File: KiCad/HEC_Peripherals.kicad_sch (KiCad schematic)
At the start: 11 parts, among them J2 Conn_02x12_Odd_Even, J4 Mini-DIN-6, J5 Mini-DIN-6, J6 DE9_Plug, J7 AudioJack3, U43 74LS06, U44 74LS541, Y1 Crystal

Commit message: Add NES port
Added NES port from NES port breadboard project
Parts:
- added C31, C32: C, Capacitor_THT:C_Disc_D3.4mm_W2.1mm_P2.50mm, symbol Device:C
- added J8: NES_Port_Male, Library:NES_Port_Male_Horizontal, symbol nes-port-breadboard:NES_Port_Male
- U42: footprint (none) -> Package_DIP:DIP-40_W25.4mm_Socket
- U43: footprint (none) -> Package_DIP:DIP-14_W7.62mm_Socket
- U44: footprint (none) -> Package_DIP:DIP-20_W7.62mm_Socket
- Y1: footprint (none) -> Crystal:Crystal_HC18-U_Vertical
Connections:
- net GND: now also C31.1, C32.1, J8.1 (GND)
- net VCC: now also J8.7 (VDD)
- net at U42.2 (OSCI), Y1.1: now also C31.2
- net at U42.3 (OSCO), Y1.2: now also C32.2
- net at U42.21 (RC): now also J8.2 (CLK)
- net at U42.22 (A20): now also J8.3 (LATCH)
- net at U42.29 (P12): now also J8.4 (DATA)
- net at U42.30 (P13): now also J8.5 (D4)
- net at U42.31 (P14): now also J8.6 (D3)
- no-connect marks 11 -> 6
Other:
- moved on the sheet: J4, J5, RN5, U43A, U43B, U43C, U43D

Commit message: Removed DMA from bus
Bus-mastering DMA has been removed from the expansion bus design due to complexity and bandwidth issue with external bus expansion circuit. The pins are replaced with audio output from on-bard sound system. Minor changes to pin names.
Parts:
- removed J8: NES_Port_Male, Library:NES_Port_Male_Horizontal, symbol nes-port-breadboard:NES_Port_Male
- added J8: NES_Port_Male, symbol New_Library:NES_Port_Male
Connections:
- net GND: now also J8.1 (GND)
- net VCC: now also J8.7 (VDD)
- net AUDIO_R: now reaches J2.23 (Pin_23), J7.T
- net AUDIO_L: now reaches J2.24 (Pin_24), J7.R
- net at U42.21 (RC): now also J8.2 (CLK)
- net at U42.22 (A20): now also J8.3 (LATCH)
- net at U42.29 (P12): now also J8.4 (DATA)
- net at U42.30 (P13): now also J8.5 (D4)
- net at U42.31 (P14): now also J8.6 (D3)
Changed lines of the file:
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@@
   (junction (at 66.675 160.02) (diameter 0) (color 0 0 0 0)
   )
+  (junction (at 74.93 95.885) (diameter 0) (color 0 0 0 0)
+  )
   (junction (at 76.835 170.18) (diameter 0) (color 0 0 0 0)
   )
@@
   )
   (junction (at 71.755 165.1) (diameter 0) (color 0 0 0 0)
+  )
+  (junction (at 90.805 93.345) (diameter 0) (color 0 0 0 0)
   )
   (junction (at 241.3 84.455) (diameter 0) (color 0 0 0 0)
@@
     (stroke (width 0) (type default))
   )
-  (wire (pts (xy 98.425 95.885) (xy 74.93 95.885))
+  (wire (pts (xy 71.755 95.885) (xy 74.93 95.885))
     (stroke (width 0) (type default))
   )
@@
     (stroke (width 0) (type default))
   )
+  (wire (pts (xy 71.755 93.345) (xy 90.805 93.345))
+    (stroke (width 0) (type default))
+  )
   (wire (pts (xy 52.07 167.64) (xy 74.295 167.64))
     (stroke (width 0) (type default))
@@
   )
   (wire (pts (xy 133.35 96.52) (xy 133.35 104.14))
+    (stroke (width 0) (type default))
+  )
+  (wire (pts (xy 74.93 95.885) (xy 98.425 95.885))
     (stroke (width 0) (type default))
   )
@@
     (effects (font (size 1.27 1.27)) (justify right))
   )
+  (hierarchical_label "AUDIO_L" (shape output) (at 71.755 93.345 180) (fields_autoplaced)
+    (effects (font (size 1.27 1.27)) (justify right))
+  )
   (hierarchical_label "A[0..4]" (shape input) (at 41.275 56.515 180) (fields_autoplaced)
     (effects (font (size 1.27 1.27)) (justify right))
@@
   )
   (hierarchical_label "~{MS_IRQ}" (shape output) (at 129.54 90.17 180) (fields_autoplaced)
+    (effects (font (size 1.27 1.27)) (justify right))
+  )
+  (hierarchical_label "AUDIO_R" (shape output) (at 71.755 95.885 180) (fields_autoplaced)
     (effects (font (size 1.27 1.27)) (justify right))
   )
@@
     )
   )
+  (symbol (lib_id "New_Library:NES_Port_Male") (at 210.82 33.655 0) (unit 1)
+    (in_bom yes) (on_board yes) (dnp no) (fields_autoplaced)
+    (property "Reference" "J8" (at 210.82 24.13 0)
+      (effects (font (size 1.27 1.27)))
+    )
+    (property "Value" "NES_Port_Male" (at 210.82 26.67 0)
+      (effects (font (size 1.27 1.27)))
+    )
+    (property "Footprint" "" (at 238.76 31.115 0)
+      (effects (font (size 1.27 1.27)) hide)
+    )
+    (property "Datasheet" "" (at 238.76 31.115 0)
+      (effects (font (size 1.27 1.27)) hide)
+    )
+    (pin "1")
+    (pin "2")
+    (pin "3")
+    (pin "4")
+    (pin "5")
+    (pin "6")
+    (pin "7")
+    (instances
+      (project "HEC1"
+        (path "/87935374-b60a-4f41-99da-94b76103dd77/b96e4e19-77bb-438e-a98c-e547a5bf0bc4"
+          (reference "J8") (unit 1)
+        )
+      )
+    )
+  )
   (symbol (lib_id "power:GND") (at 189.23 36.195 0) (unit 1)
     (in_bom yes) (on_board yes) (dnp no) (fields_autoplaced)
@@
         )
       )
-    )
-  )
-  (symbol (lib_id "nes-port-breadboard:NES_Port_Male") (at 210.82 33.655 0) (unit 1)
-    (in_bom yes) (on_board yes) (dnp no) (fields_autoplaced)
-    (property "Reference" "J8" (at 210.82 23.495 0)
-      (effects (font (size 1.27 1.27)))
-    )
-    (property "Value" "NES_Port_Male" (at 210.82 26.035 0)
-      (effects (font (size 1.27 1.27)))
-    )
-    (property "Footprint" "Library:NES_Port_Male_Horizontal" (at 238.76 31.115 0)
-      (effects (font (size 1.27 1.27)) hide)
-    )
-    (property "Datasheet" "" (at 238.76 31.115 0)
-      (effects (font (size 1.27 1.27)) hide)
-    )
-    (pin "1")
-    (pin "2")
-    (pin "3")
-    (pin "4")
-    (pin "5")
-    (pin "6")
-    (pin "7")
-    (instances
-      (project "HEC1"
-        (path "/87935374-b60a-4f41-99da-94b76103dd77/b96e4e19-77bb-438e-a98c-e547a5bf0bc4"
-          (reference "J8") (unit 1)
-        )
-      )

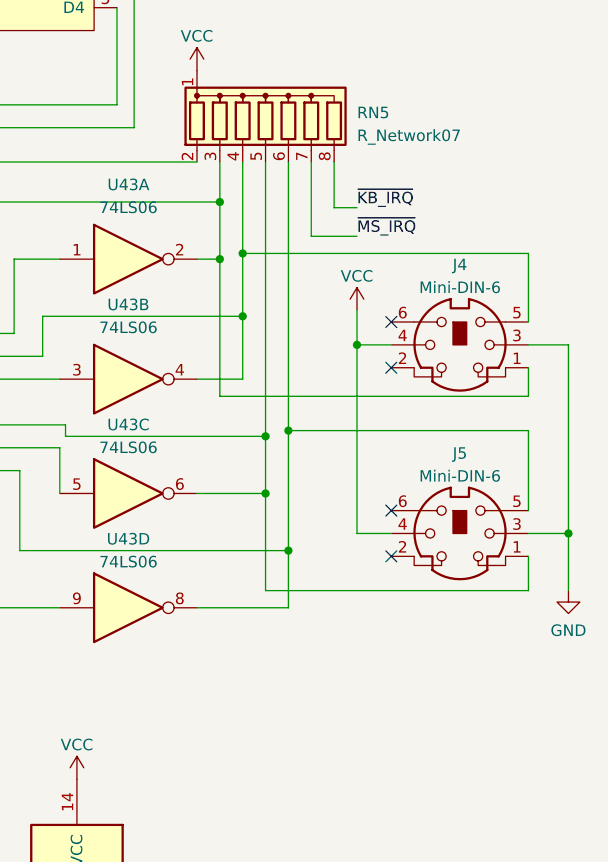
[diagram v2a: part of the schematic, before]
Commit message: Add Mini-DIN-6 footprint
It turns out that KiCad had only symbol but not footprint for Mini-DIN-6. Therefore I used a custom one made by 4x1md
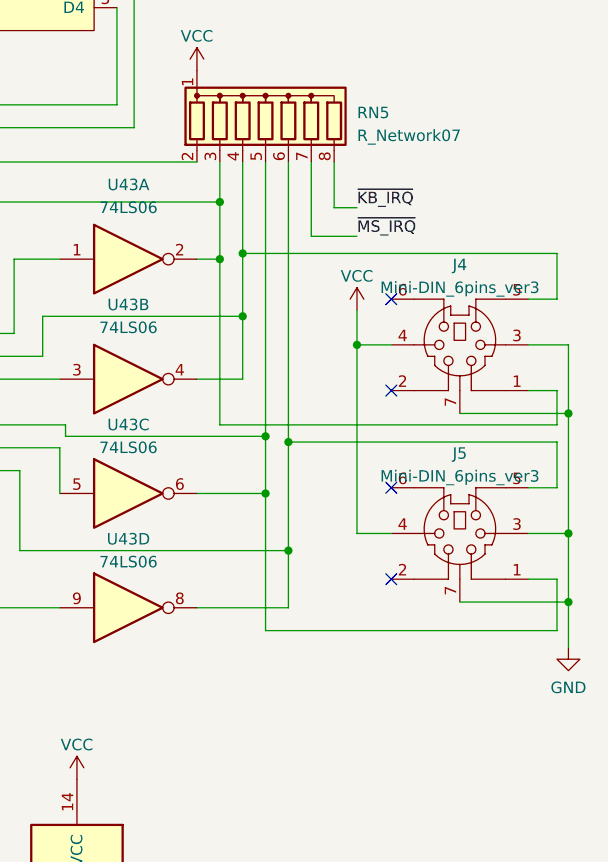
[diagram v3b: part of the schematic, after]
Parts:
- removed J4, J5: Mini-DIN-6, symbol Connector:Mini-DIN-6
- added J4, J5: Mini-DIN_6pins_ver3, Library:Connector_Mini-DIN_Female_6Pin_2rows, symbol New_Library:Mini-DIN_6pins_ver3
- J8: footprint (none) -> Library:NES_Port_Male_Horizontal
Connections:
- net GND: now also J4.3, J4.7 (Shell), J5.3, J5.7 (Shell)
- net VCC: now also J4.4, J5.4
- net at RN5.3 (R2), U42.28 (P11/MSDI), U43.2: now also J4.1
- net at RN5.4 (R3), U42.39 (KBDI/MSCI), U43.4: now also J4.5
- net at RN5.5 (R4), U42.27 (P10/KBDI), U43.6: now also J5.1
- net at RN5.6 (R5), U42.1 (KBCI), U43.8: now also J5.5

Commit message: PCB Layout attempt
Played with PCB layout a bit to get an idea of how the layout of HEC would look like. Minor updates to schematic to simplify  PCB layout.
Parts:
- removed J6: DE9_Plug, Connector_Dsub:DSUB-9_Female_Horizontal_P2.77x2.54mm_EdgePinOffset9.40mm, symbol Connector:DE9_Plug
- added J6: DE9_Plug_MountingHoles, Connector_Dsub:DSUB-9_Male_Horizontal_P2.77x2.84mm_EdgePinOffset4.94mm_Housed_MountingHolesOffset7.48mm, symbol Connector:DE9_Plug_MountingHoles
- U42: footprint Package_DIP:DIP-40_W25.4mm_Socket -> Package_DIP:DIP-40_W15.24mm_Socket
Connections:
- net GND: now also J6.0 (PAD), J6.8
- net at RN6.2 (R1), U44.2 (A0): now also J6.1
- net at RN6.3 (R2), U44.3 (A1): now also J6.2
- net at RN6.4 (R3), U44.4 (A2): now also J6.3
- net at RN6.5 (R4), U44.5 (A3): now also J6.4
- net at RN6.6 (R5), U44.6 (A4): now also J6.6
- net at RN6.7 (R6), U44.7 (A5): now also J6.5
- net at RN6.8 (R7), U44.8 (A6): now also J6.9
- net at RN6.9 (R8), U44.9 (A7): now also J6.7
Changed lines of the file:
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@@
   (junction (at 69.215 162.56) (diameter 0) (color 0 0 0 0)
+  )
+  (junction (at 41.91 178.435) (diameter 0) (color 0 0 0 0)
   )
   (junction (at 170.815 38.1) (diameter 0) (color 0 0 0 0)
@@
     (stroke (width 0) (type default))
   )
+  (wire (pts (xy 41.91 160.02) (xy 41.91 178.435))
+    (stroke (width 0) (type default))
+  )
   (wire (pts (xy 215.9 86.36) (xy 215.9 91.44))
     (stroke (width 0) (type default))
@@
     (stroke (width 0) (type default))
   )
+  (wire (pts (xy 33.02 178.435) (xy 33.02 177.8))
+    (stroke (width 0) (type default))
+  )
   (wire (pts (xy 236.22 78.74) (xy 231.14 78.74))
     (stroke (width 0) (type default))
@@
     (stroke (width 0) (type default))
   )
-  (wire (pts (xy 41.91 160.02) (xy 41.91 175.26))
-    (stroke (width 0) (type default))
-  )
   (wire (pts (xy 88.9 76.835) (xy 93.98 76.835))
     (stroke (width 0) (type default))
@@
     (stroke (width 0) (type default))
   )
+  (wire (pts (xy 41.91 178.435) (xy 33.02 178.435))
+    (stroke (width 0) (type default))
+  )
   (wire (pts (xy 193.675 32.385) (xy 199.39 32.385))
     (stroke (width 0) (type default))
@@
   )
   (wire (pts (xy 132.715 74.93) (xy 132.715 78.105))
+    (stroke (width 0) (type default))
+  )
+  (wire (pts (xy 41.91 178.435) (xy 41.91 181.61))
     (stroke (width 0) (type default))
   )
@@
     )
   )
-  (symbol (lib_id "power:GND") (at 41.91 175.26 0) (unit 1)
-    (in_bom yes) (on_board yes) (dnp no) (fields_autoplaced)
-    (property "Reference" "#PWR0121" (at 41.91 181.61 0)
-      (effects (font (size 1.27 1.27)) hide)
-    )
-    (property "Value" "GND" (at 41.91 180.34 0)
-      (effects (font (size 1.27 1.27)))
-    )
-    (property "Footprint" "" (at 41.91 175.26 0)
-      (effects (font (size 1.27 1.27)) hide)
-    )
-    (property "Datasheet" "" (at 41.91 175.26 0)
+  (symbol (lib_id "power:GND") (at 41.91 181.61 0) (unit 1)
+    (in_bom yes) (on_board yes) (dnp no) (fields_autoplaced)
+    (property "Reference" "#PWR0121" (at 41.91 187.96 0)
+      (effects (font (size 1.27 1.27)) hide)
+    )
+    (property "Value" "GND" (at 41.91 186.69 0)
+      (effects (font (size 1.27 1.27)))
+    )
+    (property "Footprint" "" (at 41.91 181.61 0)
+      (effects (font (size 1.27 1.27)) hide)
+    )
+    (property "Datasheet" "" (at 41.91 181.61 0)
       (effects (font (size 1.27 1.27)) hide)
     )
@@
     )
   )
+  (symbol (lib_id "Connector:DE9_Plug_MountingHoles") (at 33.02 162.56 0) (mirror y) (unit 1)
+    (in_bom yes) (on_board yes) (dnp no) (fields_autoplaced)
+    (property "Reference" "J6" (at 33.02 144.78 0)
+      (effects (font (size 1.27 1.27)))
+    )
+    (property "Value" "DE9_Plug_MountingHoles" (at 33.02 147.32 0)
+      (effects (font (size 1.27 1.27)))
+    )
+    (property "Footprint" "Connector_Dsub:DSUB-9_Male_Horizontal_P2.77x2.84mm_EdgePinOffset4.94mm_Housed_MountingHolesOffset7.48mm" (at 33.02 162.56 0)
+      (effects (font (size 1.27 1.27)) hide)
+    )
+    (property "Datasheet" " ~" (at 33.02 162.56 0)
+      (effects (font (size 1.27 1.27)) hide)
+    )
+    (pin "0")
+    (pin "1")
+    (pin "2")
+    (pin "3")
+    (pin "4")
+    (pin "5")
+    (pin "6")
+    (pin "7")
+    (pin "8")
+    (pin "9")
+    (instances
+      (project "HEC1"
+        (path "/87935374-b60a-4f41-99da-94b76103dd77/b96e4e19-77bb-438e-a98c-e547a5bf0bc4"
+          (reference "J6") (unit 1)
+        )
+      )
+    )
+  )
   (symbol (lib_id "74xx:74LS06") (at 223.52 91.44 0) (unit 3)
     (in_bom yes) (on_board yes) (dnp no) (fields_autoplaced)
@@
       (effects (font (size 1.27 1.27)))
     )
-    (property "Footprint" "Package_DIP:DIP-40_W25.4mm_Socket" (at 170.815 76.2 0)
+    (property "Footprint" "Package_DIP:DIP-40_W15.24mm_Socket" (at 170.815 76.2 0)
       (effects (font (size 1.27 1.27)) hide)
     )
@@
         )
       )
-    )
-  )
-  (symbol (lib_id "Connector:DE9_Plug") (at 33.02 162.56 0) (mirror y) (unit 1)
-    (in_bom yes) (on_board yes) (dnp no) (fields_autoplaced)
-    (property "Reference" "J6" (at 33.02 144.78 0)
-      (effects (font (size 1.27 1.27)))
-    )
-    (property "Value" "DE9_Plug" (at 33.02 147.32 0)
-      (effects (font (size 1.27 1.27)))
-    )
-    (property "Footprint" "Connector_Dsub:DSUB-9_Female_Horizontal_P2.77x2.54mm_EdgePinOffset9.40mm" (at 33.02 162.56 0)
-      (effects (font (size 1.27 1.27)) hide)
-    )
-    (property "Datasheet" " ~" (at 33.02 162.56 0)
-      (effects (font (size 1.27 1.27)) hide)
-    )
-    (pin "1")
-    (pin "2")
-    (pin "3")
-    (pin "4")
-    (pin "5")
-    (pin "6")
-    (pin "7")
-    (pin "8")
-    (pin "9")
-    (instances
-      (project "HEC1"
-        (path "/87935374-b60a-4f41-99da-94b76103dd77/b96e4e19-77bb-438e-a98c-e547a5bf0bc4"
-          (reference "J6") (unit 1)
-        )
-      )

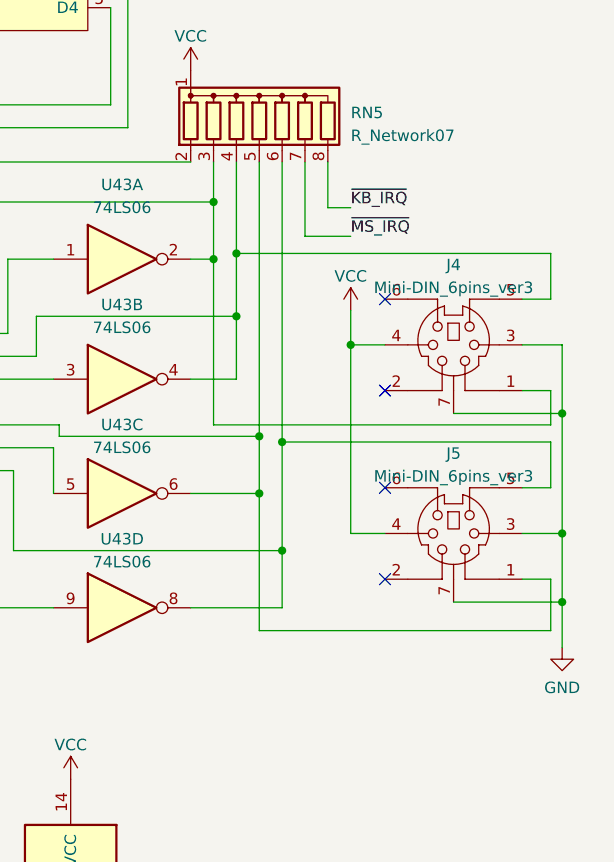
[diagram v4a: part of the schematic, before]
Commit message: double Mini DIN 6 port
Added double Mini DIN 6 port to replace two Mini DIN 6 port to save cost and simplify building process. The footprint is derived from the existing single mini DIN 6 port. With changes according to the png schematic. This is my first attempt at creating a footprint beyond simple 0.1inch pads, so it may be wrong. Minor changes to the PCB.
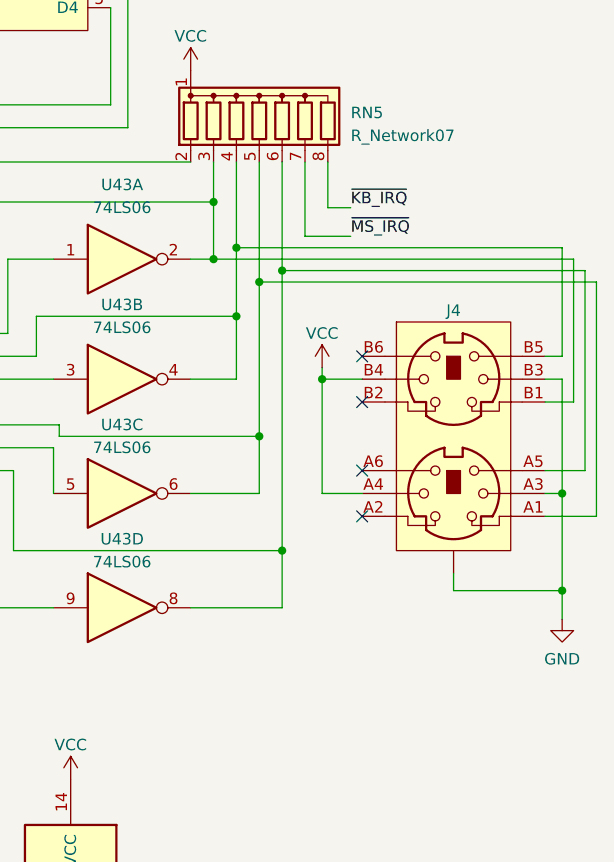
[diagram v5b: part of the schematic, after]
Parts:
- removed J4, J5: Mini-DIN_6pins_ver3, Library:Connector_Mini-DIN_Female_6Pin_2rows, symbol New_Library:Mini-DIN_6pins_ver3
- added J4: ~, symbol New_Library:double_mini-DIN_6
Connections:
- net GND: now also J4., J4.A3, J4.B3
- net VCC: now also J4.A4, J4.B4
- net at RN5.3 (R2), U42.28 (P11/MSDI), U43.2: now also J4.B1
- net at RN5.4 (R3), U42.39 (KBDI/MSCI), U43.4: now also J4.B5
- net at RN5.5 (R4), U42.27 (P10/KBDI), U43.6: now also J4.A1
- net at RN5.6 (R5), U42.1 (KBCI), U43.8: now also J4.A5
